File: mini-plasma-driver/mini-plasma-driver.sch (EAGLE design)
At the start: 78 parts, among them IC1 IR21844D, IC2 74LS19N, IC3 NE555N, IC5 IR21844D, Q1 IRF640, Q2 IRF640, Q3 2N2369, Q4 2N2369, Q5 IRF640, Q6 IRF640

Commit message: change D5/D6 to vertical footprint
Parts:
- D5, D6: device diode:MUR150RL -> keves-ng:VERTICAL-DIODE

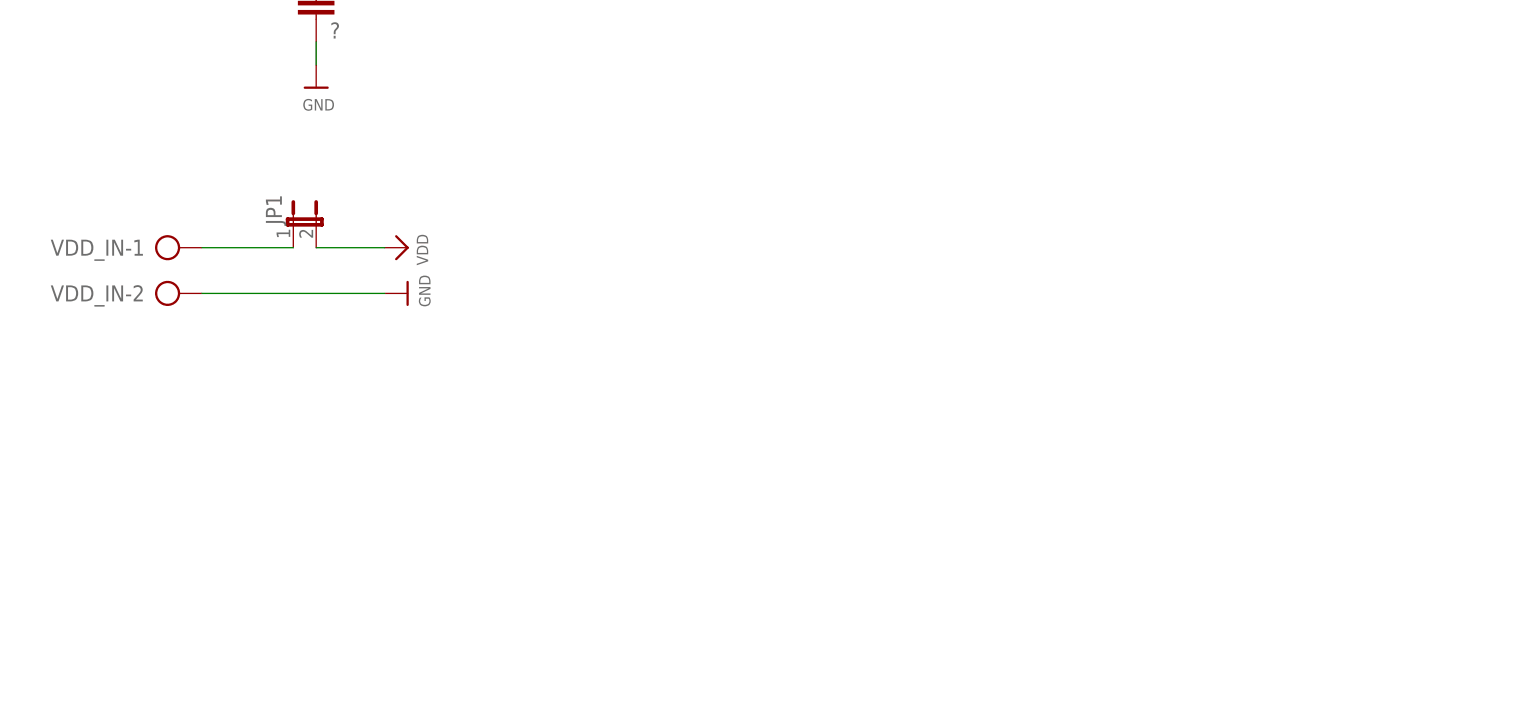
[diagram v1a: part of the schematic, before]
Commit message: added Line input for VDD
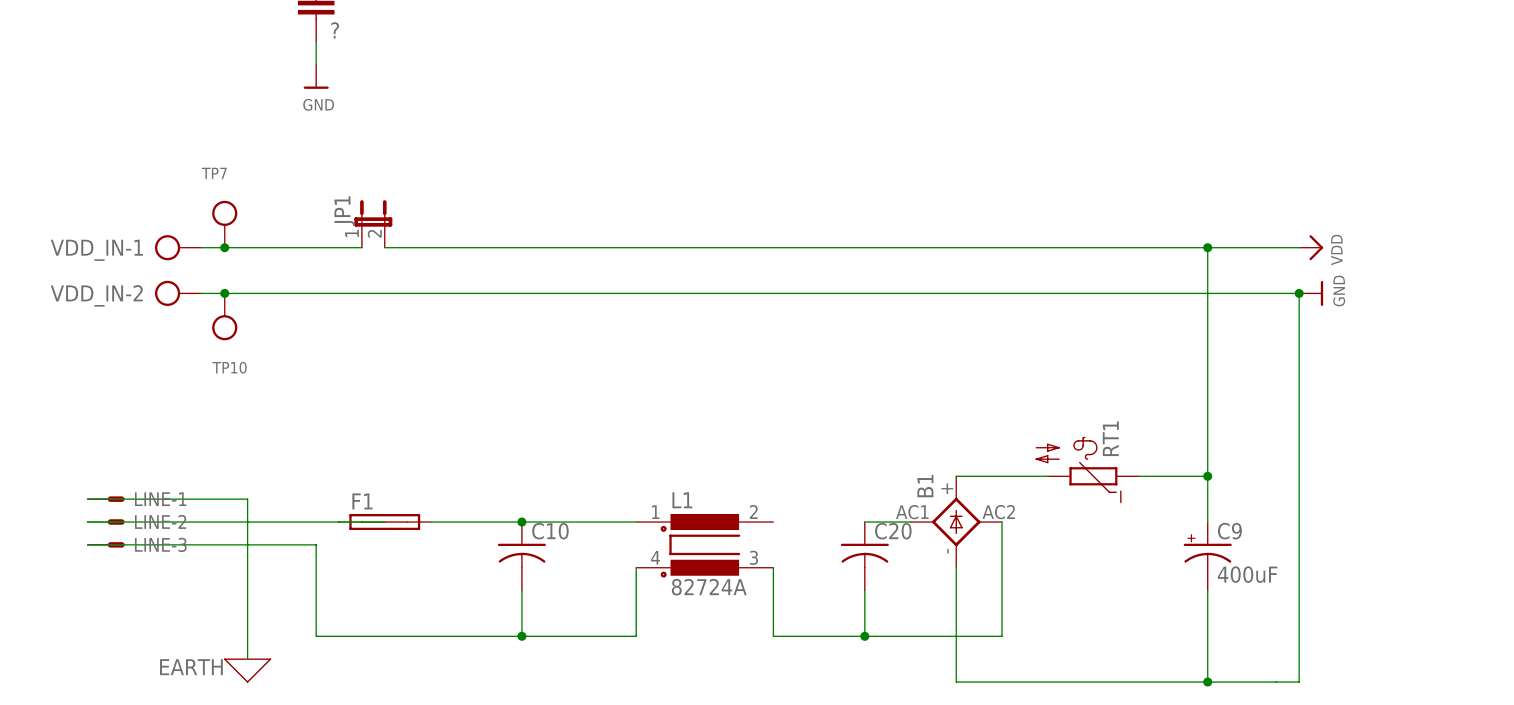
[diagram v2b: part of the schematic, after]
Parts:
- added B1: (no value), rectifier:2KBB-R
- added C10, C20: (no value), rcl:C-US150-084X183
- added C9: 400uF, rcl:CPOL-USE7.5-18
- added F1: (no value), fuse:SH22,5A
- added L1: 82724A, inductors:82724A
- added LINE: (no value), con-molex:KK-156-3
- added RT1: (no value), ptc-ntc:B57164
- added TP10, TP7: (no value), microbuilder:TESTPOINT0.1"
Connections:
- new net EARTH: LINE-1.S
- new net N$18: C10.1, F1.2, L1.1
- new net N$19: F1.1, LINE-2.S
- new net N$20: B1.AC1, C20.1
- new net N$22: C10.2, L1.3, LINE-3.S
- new net N$25: B1.+, RT1.2
- new net N$31: B1.AC2, C20.2, L1.4
- net GND: now also B1.-, C9.-, TP10.P$1
- net N$33: now also TP7.P$1
- net VDD: now also C9.+, RT1.1
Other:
- moved on the sheet: JP1
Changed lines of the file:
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@@
 <part name="D5" library="keves-ng" deviceset="VERTICAL-DIODE" device="" package3d_urn="urn:adsk.eagle:package:23572/1" value="MUR120"/>
 <part name="D6" library="keves-ng" deviceset="VERTICAL-DIODE" device="" package3d_urn="urn:adsk.eagle:package:23572/1" value="MUR120"/>
+<part name="TP7" library="microbuilder" deviceset="TESTPOINT" device="0.1&quot;"/>
+<part name="TP10" library="microbuilder" deviceset="TESTPOINT" device="0.1&quot;"/>
+<part name="LINE" library="con-molex" library_urn="urn:adsk.eagle:library:165" deviceset="KK-156-3" device=""/>
+<part name="F1" library="fuse" library_urn="urn:adsk.eagle:library:233" deviceset="SH22,5A" device="" package3d_urn="urn:adsk.eagle:package:14070/1"/>
+<part name="C9" library="rcl" library_urn="urn:adsk.eagle:library:334" deviceset="CPOL-US" device="E7.5-18" package3d_urn="urn:adsk.eagle:package:23379/1" value="400uF"/>
+<part name="C10" library="rcl" library_urn="urn:adsk.eagle:library:334" deviceset="C-US" device="150-084X183" package3d_urn="urn:adsk.eagle:package:23658/1"/>
+<part name="C20" library="rcl" library_urn="urn:adsk.eagle:library:334" deviceset="C-US" device="150-084X183" package3d_urn="urn:adsk.eagle:package:23658/1"/>
+<part name="L1" library="inductors" library_urn="urn:adsk.eagle:library:243" deviceset="82724A" device="" package3d_urn="urn:adsk.eagle:package:15058/1"/>
+<part name="B1" library="rectifier" library_urn="urn:adsk.eagle:library:336" deviceset="2KBB-R" device="" package3d_urn="urn:adsk.eagle:package:23895/1"/>
+<part name="X_1" library="ngspice-simulation" library_urn="urn:adsk.eagle:library:527439" deviceset="GND" device=""/>
+<part name="RT1" library="ptc-ntc" library_urn="urn:adsk.eagle:library:332" deviceset="B57164" device="" package3d_urn="urn:adsk.eagle:package:22760/1"/>
 </parts>
 <sheets>
@@
 <instance part="VDD_IN" gate="-1" x="-93.98" y="7.62"/>
 <instance part="VDD_IN" gate="-2" x="-93.98" y="2.54"/>
-<instance part="JP1" gate="A" x="-78.74" y="10.16"/>
-<instance part="U$4" gate="G$1" x="-66.04" y="7.62" rot="R270"/>
-<instance part="GND15" gate="G$1" x="-66.04" y="2.54" rot="R90"/>
+<instance part="JP1" gate="A" x="-71.12" y="10.16"/>
+<instance part="U$4" gate="G$1" x="35.56" y="7.62" rot="R270"/>
+<instance part="GND15" gate="G$1" x="35.56" y="2.54" rot="R90"/>
 <instance part="TP8" gate="G$1" x="-76.2" y="55.88" rot="R270"/>
 <instance part="TP9" gate="G$1" x="-76.2" y="71.12" rot="R270"/>
@@
 <instance part="D5" gate="G$1" x="93.98" y="132.08"/>
 <instance part="D6" gate="G$1" x="93.98" y="68.58"/>
+<instance part="TP7" gate="G$1" x="-86.36" y="7.62"/>
+<instance part="TP10" gate="G$1" x="-86.36" y="2.54" rot="R180"/>
+<instance part="LINE" gate="-1" x="-99.06" y="-20.32"/>
+<instance part="LINE" gate="-2" x="-99.06" y="-22.86"/>
+<instance part="LINE" gate="-3" x="-99.06" y="-25.4"/>
+<instance part="F1" gate="1" x="-68.58" y="-22.86"/>
+<instance part="C9" gate="G$1" x="22.86" y="-25.4"/>
+<instance part="C10" gate="G$1" x="-53.34" y="-25.4"/>
+<instance part="C20" gate="G$1" x="-15.24" y="-25.4"/>
+<instance part="L1" gate="1" x="-33.02" y="-25.4"/>
+<instance part="B1" gate="1" x="-5.08" y="-22.86" rot="R90"/>
+<instance part="X_1" gate="G$1" x="-83.82" y="-38.1"/>
+<instance part="RT1" gate="1" x="10.16" y="-17.78" rot="R90"/>
 </instances>
 <busses>
@@
 <pinref part="VDD_IN" gate="-2" pin="KL"/>
 <pinref part="GND15" gate="G$1" pin="GND"/>
-<wire x1="-68.58" y1="2.54" x2="-88.9" y2="2.54" width="0.1524" layer="91"/>
+<wire x1="33.02" y1="2.54" x2="-86.36" y2="2.54" width="0.1524" layer="91"/>
+<pinref part="TP10" gate="G$1" pin="P$1"/>
+<wire x1="-86.36" y1="2.54" x2="-88.9" y2="2.54" width="0.1524" layer="91"/>
+<junction x="-86.36" y="2.54"/>
+<wire x1="33.02" y1="2.54" x2="33.02" y2="-40.64" width="0.1524" layer="91"/>
+<junction x="33.02" y="2.54"/>
+<pinref part="C9" gate="G$1" pin="-"/>
+<wire x1="22.86" y1="-30.48" x2="22.86" y2="-40.64" width="0.1524" layer="91"/>
+<wire x1="33.02" y1="-40.64" x2="30.48" y2="-40.64" width="0.1524" layer="91"/>
+<wire x1="30.48" y1="-40.64" x2="22.86" y2="-40.64" width="0.1524" layer="91"/>
+<pinref part="B1" gate="1" pin="-"/>
+<wire x1="-5.08" y1="-27.94" x2="-5.08" y2="-40.64" width="0.1524" layer="91"/>
+<wire x1="-5.08" y1="-40.64" x2="22.86" y2="-40.64" width="0.1524" layer="91"/>
+<junction x="22.86" y="-40.64"/>
 </segment>
 <segment>
@@
 <pinref part="JP1" gate="A" pin="2"/>
 <pinref part="U$4" gate="G$1" pin="VDD"/>
-<wire x1="-68.58" y1="7.62" x2="-76.2" y2="7.62" width="0.1524" layer="91"/>
+<wire x1="33.02" y1="7.62" x2="22.86" y2="7.62" width="0.1524" layer="91"/>
+<pinref part="C9" gate="G$1" pin="+"/>
+<pinref part="RT1" gate="1" pin="1"/>
+<wire x1="22.86" y1="7.62" x2="-68.58" y2="7.62" width="0.1524" layer="91"/>
+<wire x1="15.24" y1="-17.78" x2="22.86" y2="-17.78" width="0.1524" layer="91"/>
+<wire x1="22.86" y1="-17.78" x2="22.86" y2="-22.86" width="0.1524" layer="91"/>
+<wire x1="22.86" y1="-17.78" x2="22.86" y2="7.62" width="0.1524" layer="91"/>
+<junction x="22.86" y="-17.78"/>
+<junction x="22.86" y="7.62"/>
 </segment>
 </net>
@@
 <pinref part="VDD_IN" gate="-1" pin="KL"/>
 <pinref part="JP1" gate="A" pin="1"/>
-<wire x1="-78.74" y1="7.62" x2="-88.9" y2="7.62" width="0.1524" layer="91"/>
+<wire x1="-71.12" y1="7.62" x2="-86.36" y2="7.62" width="0.1524" layer="91"/>
+<pinref part="TP7" gate="G$1" pin="P$1"/>
+<wire x1="-86.36" y1="7.62" x2="-88.9" y2="7.62" width="0.1524" layer="91"/>
+<junction x="-86.36" y="7.62"/>
 </segment>
 </net>
@@
 </segment>
 </net>
+<net name="N$19" class="0">
+<segment>
+<pinref part="LINE" gate="-2" pin="S"/>
+<pinref part="F1" gate="1" pin="1"/>
+<wire x1="-101.6" y1="-22.86" x2="-73.66" y2="-22.86" width="0.1524" layer="91"/>
+<wire x1="-68.58" y1="-22.86" x2="-73.66" y2="-22.86" width="0.1524" layer="91"/>
+</segment>
+</net>
+<net name="N$18" class="0">
+<segment>
+<pinref part="F1" gate="1" pin="2"/>
+<pinref part="C10" gate="G$1" pin="1"/>
+<wire x1="-63.5" y1="-22.86" x2="-53.34" y2="-22.86" width="0.1524" layer="91"/>
+<pinref part="L1" gate="1" pin="1"/>
+<wire x1="-53.34" y1="-22.86" x2="-40.64" y2="-22.86" width="0.1524" layer="91"/>
+<junction x="-53.34" y="-22.86"/>
+</segment>
+</net>
+<net name="N$20" class="0">
+<segment>
+<pinref part="C20" gate="G$1" pin="1"/>
+<pinref part="B1" gate="1" pin="AC1"/>
+<wire x1="-15.24" y1="-22.86" x2="-10.16" y2="-22.86" width="0.1524" layer="91"/>
+</segment>
+</net>
+<net name="N$22" class="0">
+<segment>
+<pinref part="LINE" gate="-3" pin="S"/>
+<wire x1="-101.6" y1="-25.4" x2="-76.2" y2="-25.4" width="0.1524" layer="91"/>
+<wire x1="-76.2" y1="-25.4" x2="-76.2" y2="-35.56" width="0.1524" layer="91"/>
+<wire x1="-76.2" y1="-35.56" x2="-53.34" y2="-35.56" width="0.1524" layer="91"/>
+<pinref part="C10" gate="G$1" pin="2"/>
+<wire x1="-53.34" y1="-35.56" x2="-53.34" y2="-30.48" width="0.1524" layer="91"/>
+<wire x1="-53.34" y1="-35.56" x2="-40.64" y2="-35.56" width="0.1524" layer="91"/>
+<junction x="-53.34" y="-35.56"/>
+<pinref part="L1" gate="1" pin="3"/>
+<wire x1="-40.64" y1="-35.56" x2="-40.64" y2="-27.94" width="0.1524" layer="91"/>
+</segment>
+</net>
+<net name="EARTH" class="0">
+<segment>
+<pinref part="LINE" gate="-1" pin="S"/>
+<wire x1="-101.6" y1="-20.32" x2="-83.82" y2="-20.32" width="0.1524" layer="91"/>
+<wire x1="-83.82" y1="-20.32" x2="-83.82" y2="-38.1" width="0.1524" layer="91"/>
+<pinref part="X_1" gate="G$1" pin="0"/>
+<label x="-86.36" y="-38.1" size="1.778" layer="95" rot="R180"/>
+</segment>
+</net>
+<net name="N$31" class="0">
+<segment>
+<pinref part="B1" gate="1" pin="AC2"/>
+<pinref part="L1" gate="1" pin="4"/>
+<wire x1="-25.4" y1="-27.94" x2="-25.4" y2="-35.56" width="0.1524" layer="91"/>
+<wire x1="-25.4" y1="-35.56" x2="-15.24" y2="-35.56" width="0.1524" layer="91"/>
+<pinref part="C20" gate="G$1" pin="2"/>
+<wire x1="-15.24" y1="-30.48" x2="-15.24" y2="-35.56" width="0.1524" layer="91"/>
+<junction x="-15.24" y="-35.56"/>
+<wire x1="-15.24" y1="-35.56" x2="0" y2="-35.56" width="0.1524" layer="91"/>
+<wire x1="0" y1="-35.56" x2="0" y2="-22.86" width="0.1524" layer="91"/>
+</segment>
+</net>
+<net name="N$25" class="0">
+<segment>
+<pinref part="B1" gate="1" pin="+"/>
+<pinref part="RT1" gate="1" pin="2"/>
+<wire x1="-5.08" y1="-17.78" x2="5.08" y2="-17.78" width="0.1524" layer="91"/>
+</segment>
+</net>

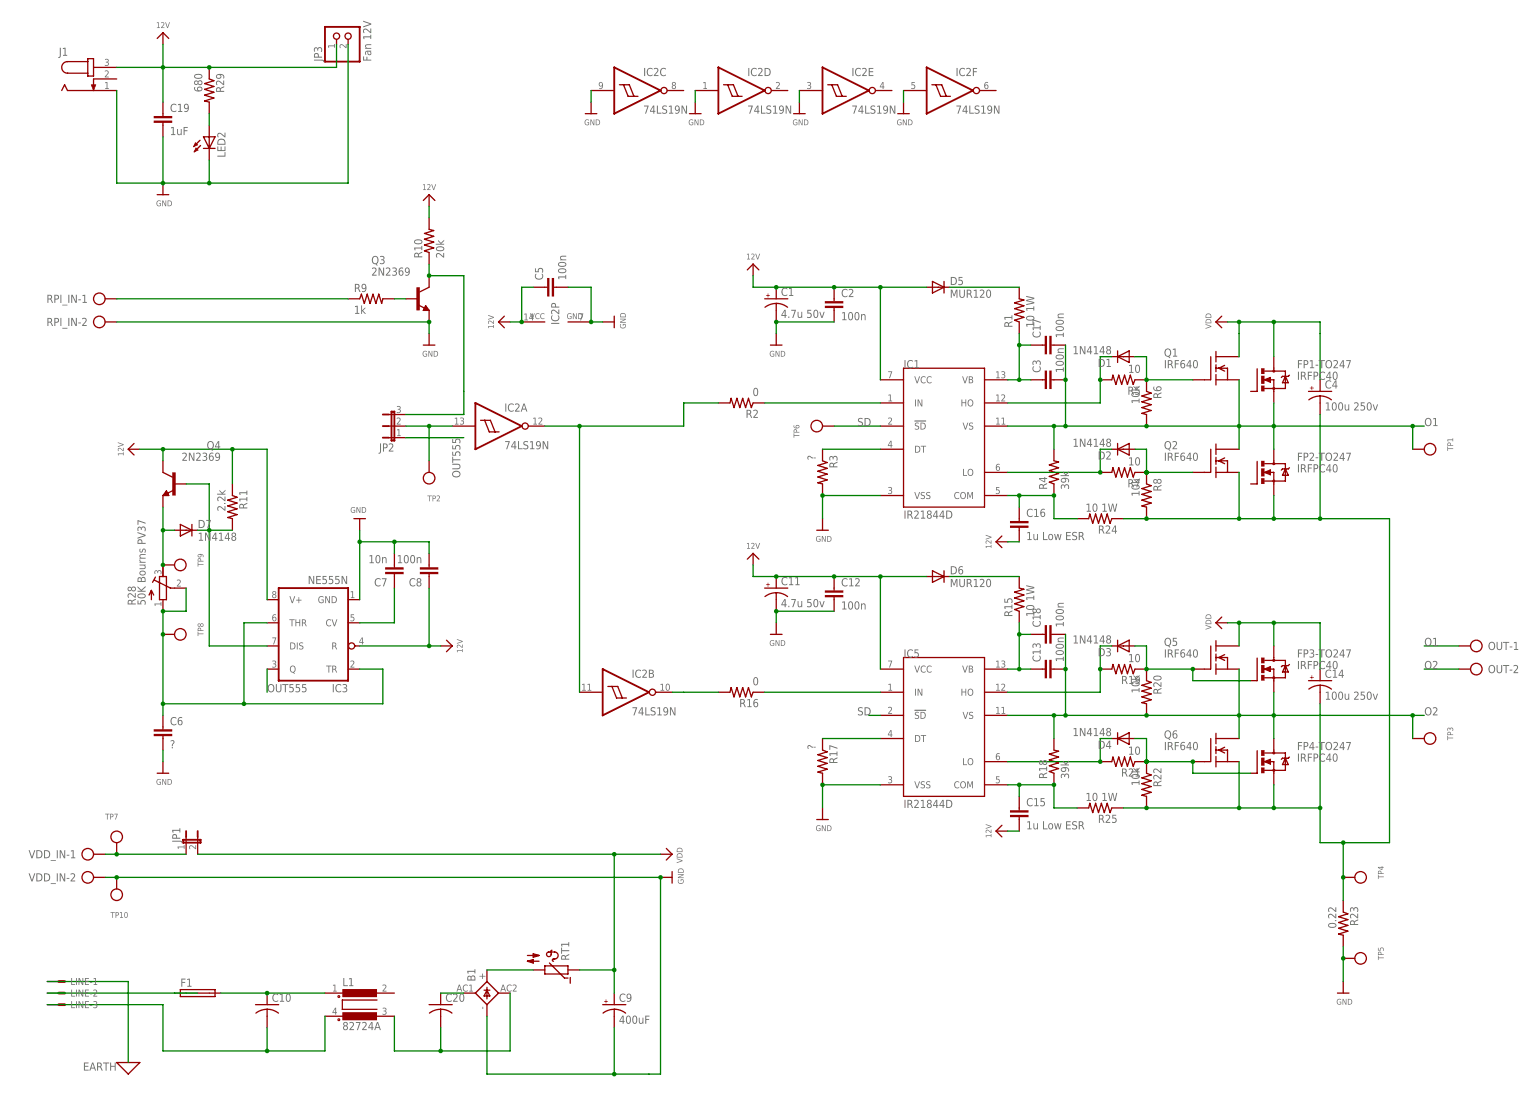
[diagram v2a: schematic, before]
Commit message: first crack at brd placement; BOM folder with data sheets
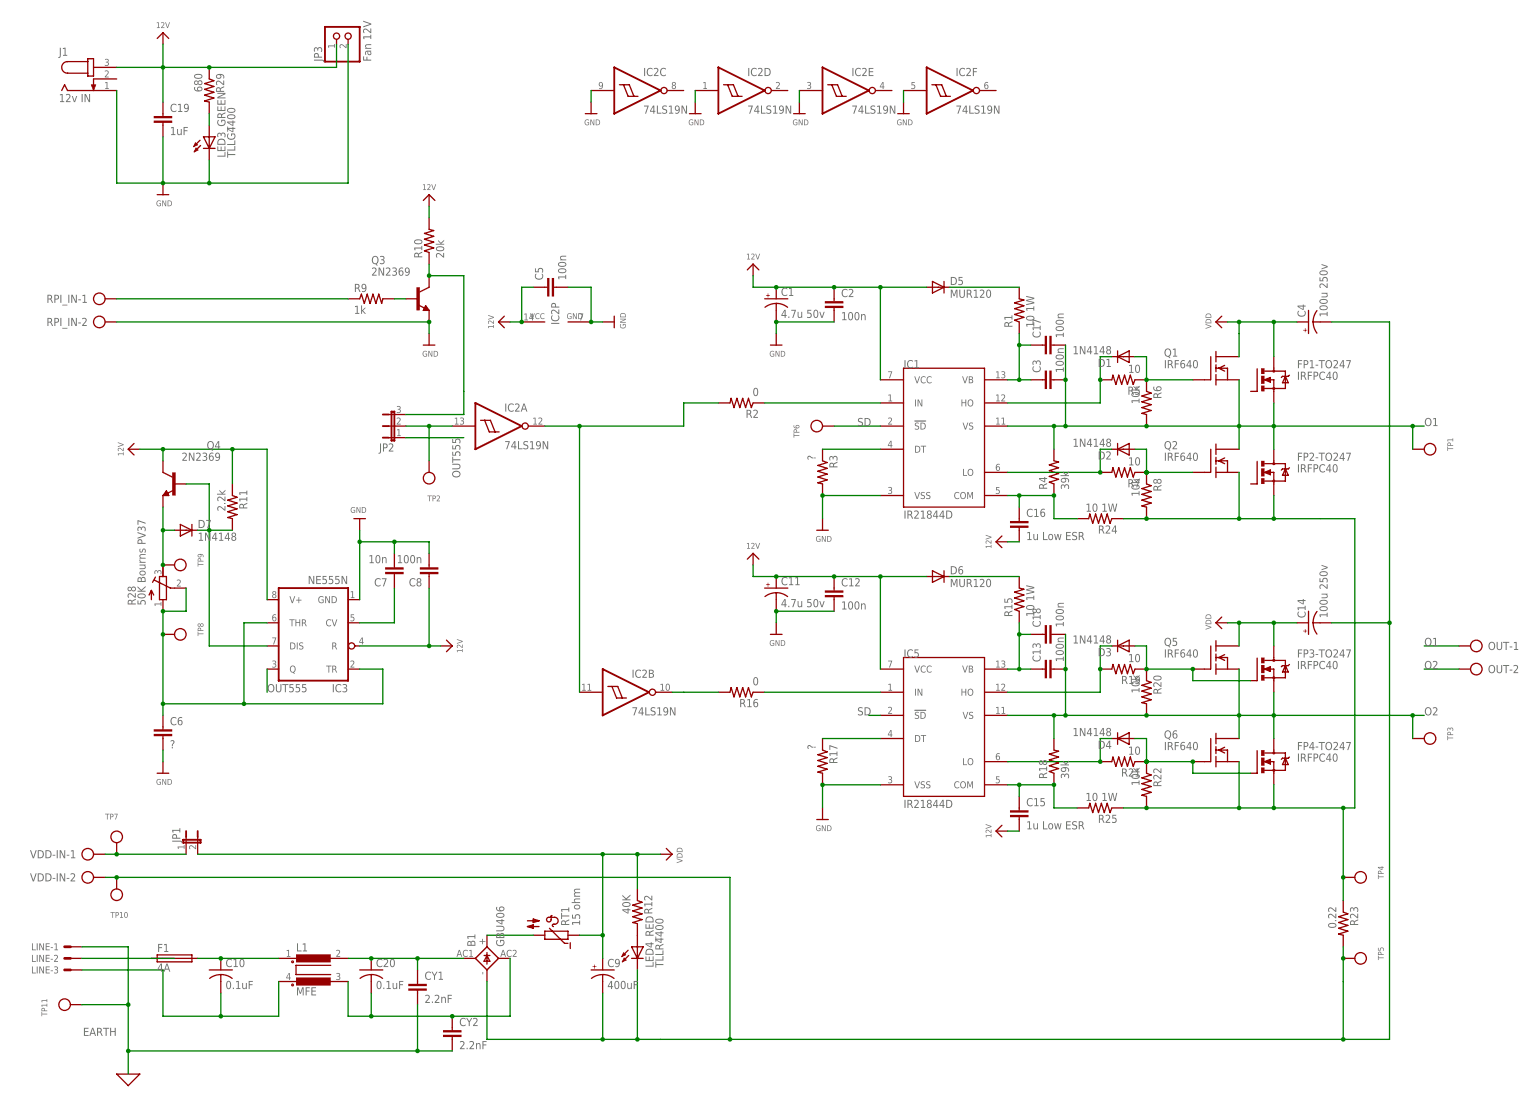
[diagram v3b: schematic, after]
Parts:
- removed LED2: (no value), led:LED5MM
- added CY1, CY2: 2.2nF, rcl:C-EU025-025X050
- added LED3_GREEN: TLLG4400, led:TLLG4400
- added LED4_RED: TLLR4400, led:TLLR4400
- added R12: 40K, rcl:R-US_0207/10
- added TP11: (no value), microbuilder:TESTPOINT0.1"
- B1: value (none) -> GBU406
- C10, C20: value (none) -> 0.1uF
- F1: value (none) -> 4A
- J1: value (none) -> 12v IN
- L1: value 82724A -> MFE; device inductors:82724A -> inductors:MFE
- RT1: value (none) -> 15 ohm
- renumbered VDD_IN to VDD-IN
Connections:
- removed net N$2: C14.-, C4.-, FP2-TO247.S, FP4-TO247.S, Q2.S, Q6.S, R22.2, R23.1, R24.1, R25.1, R8.2, TP4.P$1
- new net N$32: LED4_RED.A, R12.2
- new net N$35: FP2-TO247.S, FP4-TO247.S, Q2.S, Q6.S, R22.2, R23.1, R24.1, R25.1, R8.2, TP4.P$1
- new net VDD-: B1.-, C14.-, C4.-, C9.-, LED4_RED.C, R23.2, TP10.P$1, TP5.P$1, VDD-IN-2.KL
- net EARTH: now also CY1.2, CY2.2, TP11.P$1
- net GND: now also LED3_GREEN.C; no longer B1.-, C9.-, LED2.C, R23.2, TP10.P$1, TP5.P$1, VDD-IN-2.KL
- net N$20: now also CY1.1, L1.2
- net N$31: now also CY2.1
- net N$34: now also LED3_GREEN.A; no longer LED2.A
- net VDD: now also R12.1
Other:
- moved on the sheet: B1, C10, C14, C20, C4, C9, F1, LINE-1, LINE-2, LINE-3, RT1
